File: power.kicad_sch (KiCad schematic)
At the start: 118 parts, among them IC1 STM32MP157AAB3, IC3 STC3117IJT, IC4 MCP73830T-2AAI_MYY, IC5 MT41K256M16TW-107_P, IC6 STPMIC1BPQR, IC8 STUSB1600AQTR, J1 Conn_01x04, P1 USB_C_Plug_USB2.0, Q1 PMDPB70XP_115

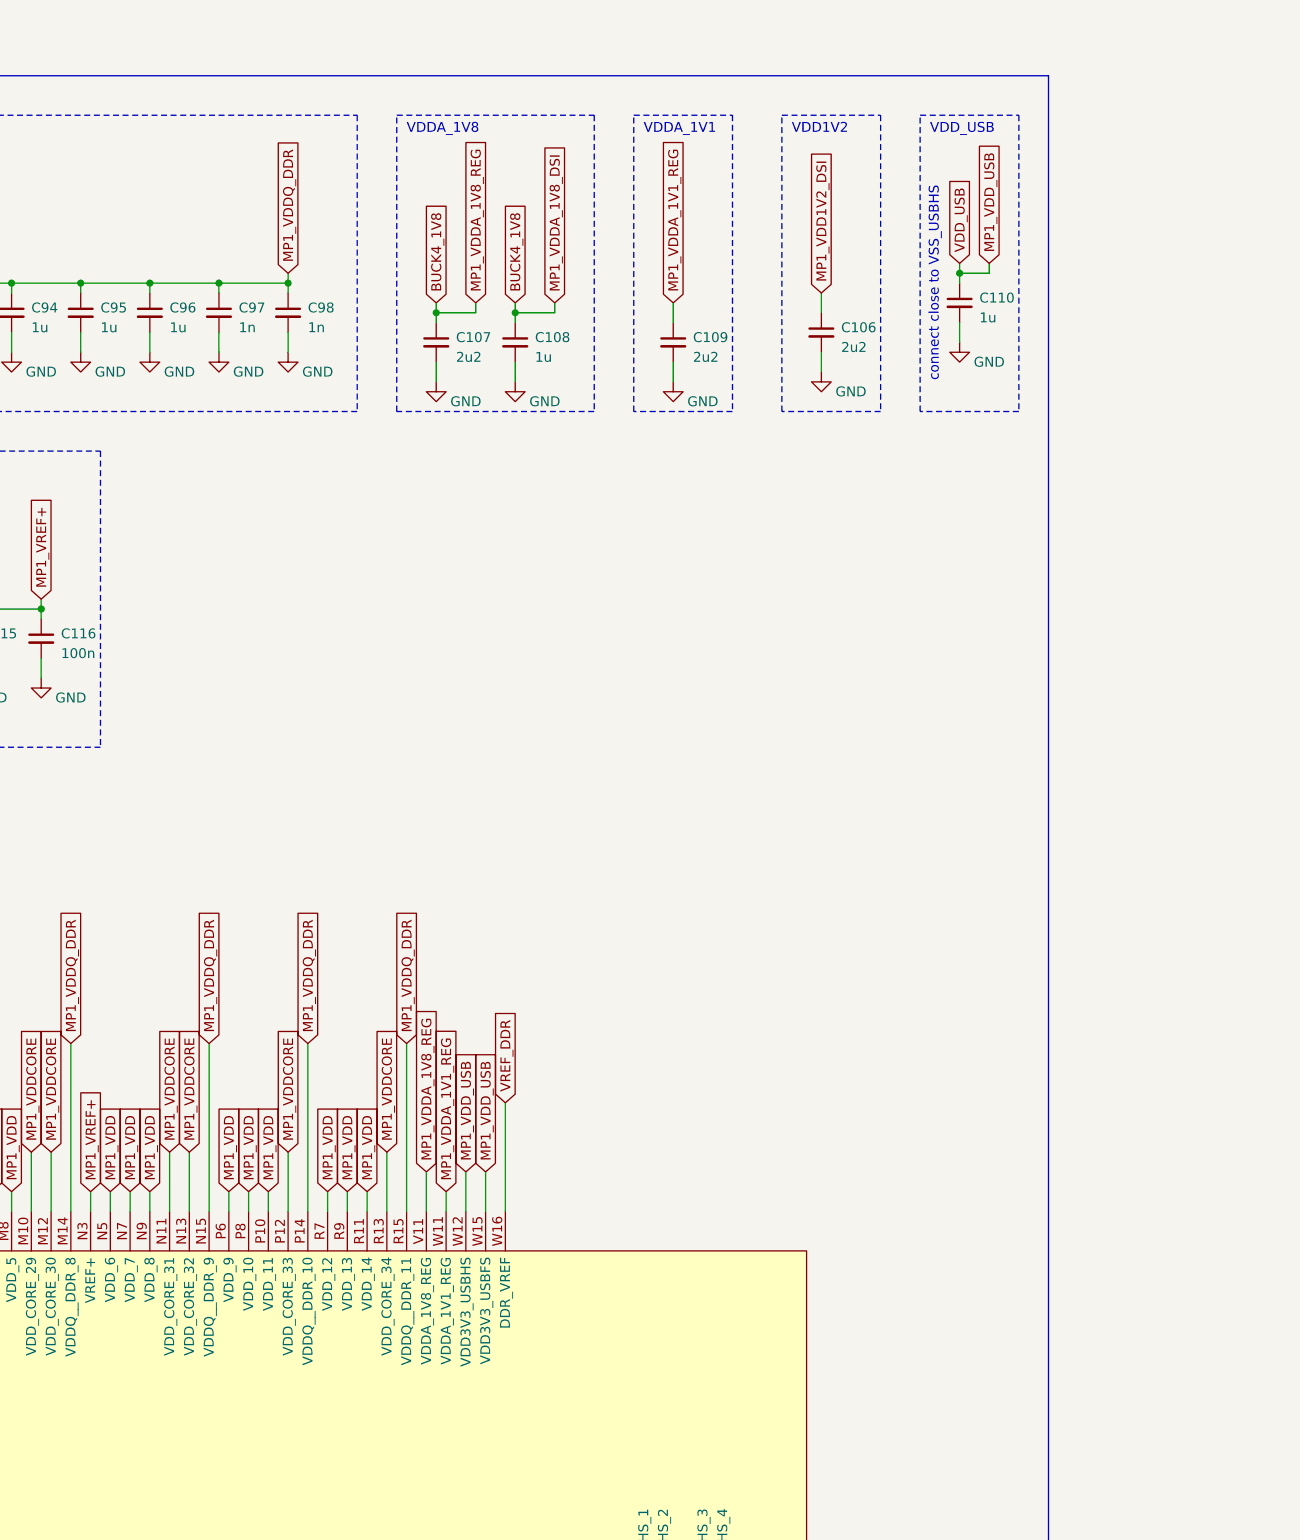
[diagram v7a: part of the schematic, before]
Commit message: changed mp1 symbol and moved BYPASS_REG1V8 signal to supply
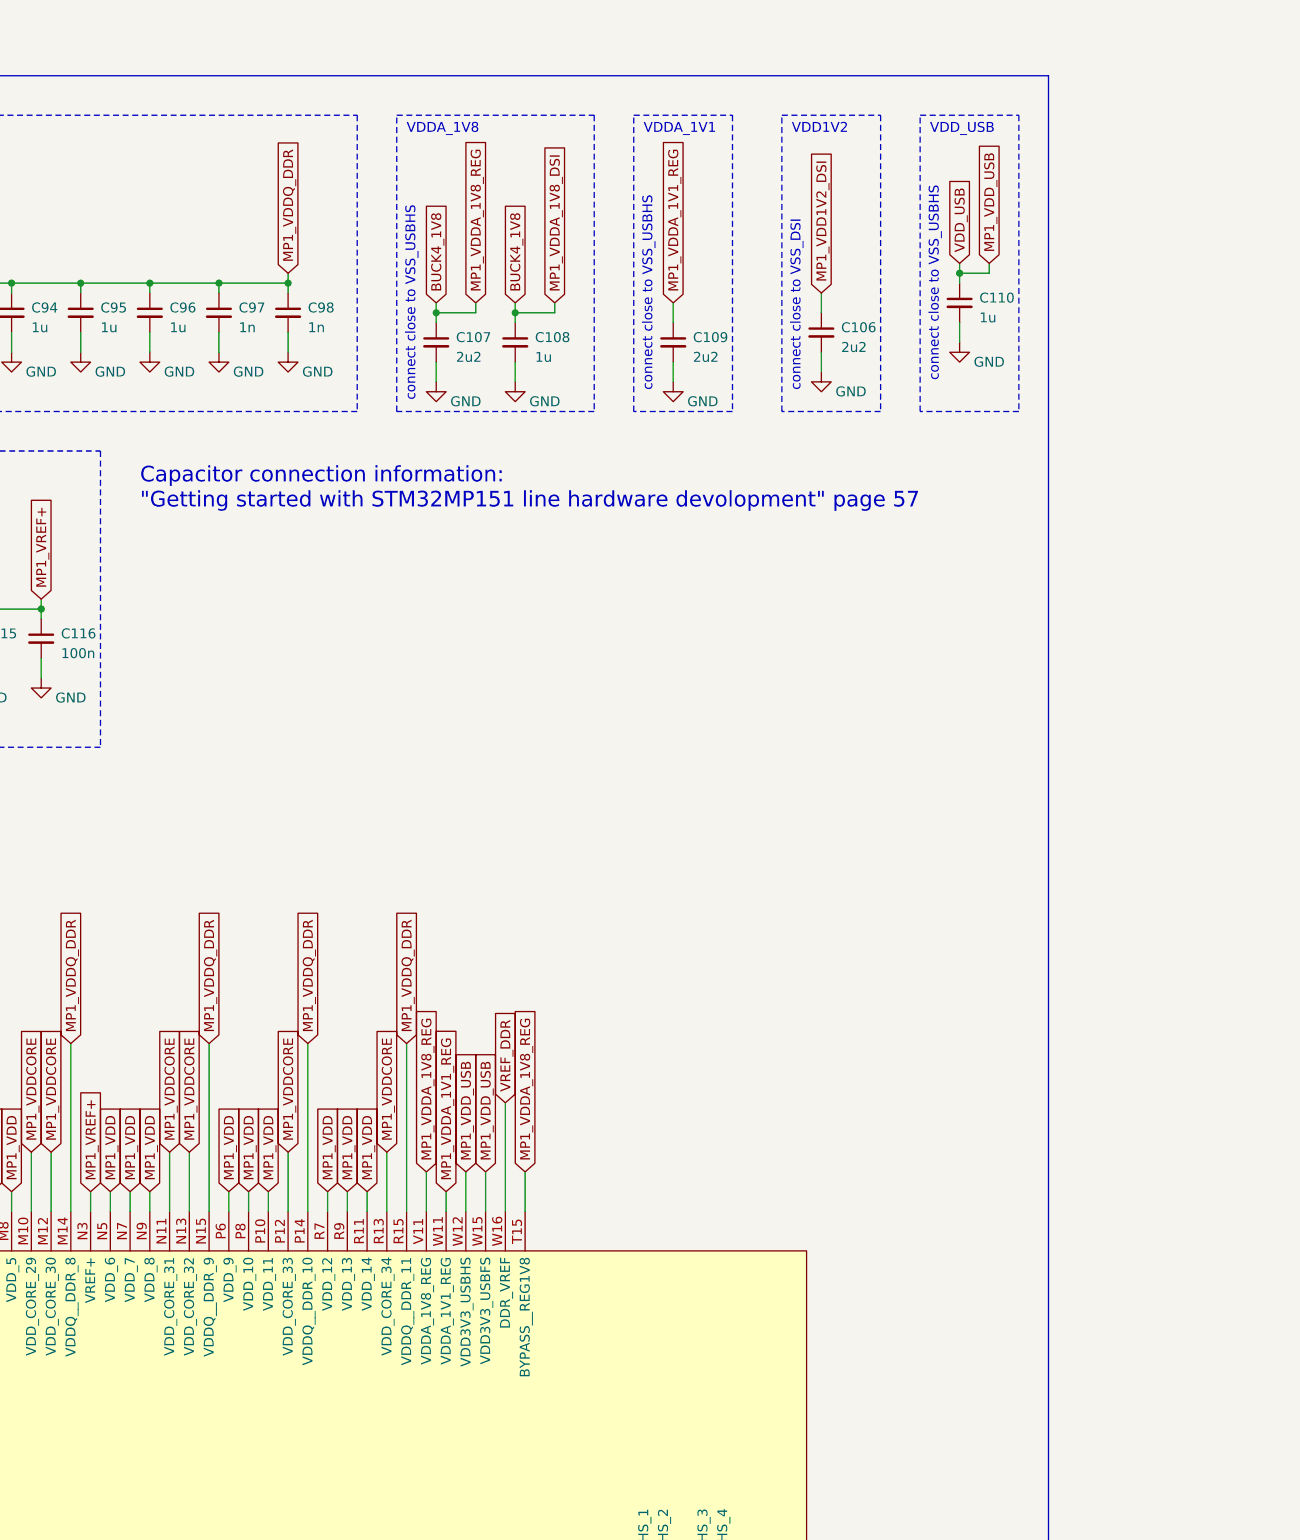
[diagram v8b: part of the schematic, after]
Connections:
- net BUCK4_1V8: now also IC1.T15 (BYPASS__REG1V8)
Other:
- note added: "Capacitor connection information: "Getting started with STM32MP151 line hardware devolopment" page 57"
- note added: "connect close to VSS_DSI"
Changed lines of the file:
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@@
     (stroke (width 0) (type default))
   )
+  (wire (pts (xy 410.21 318.77) (xy 410.21 323.85))
+    (stroke (width 0) (type default))
+  )
   (wire (pts (xy 222.25 246.38) (xy 222.25 247.65))
     (stroke (width 0) (type default))
@@
     (effects (font (size 1.27 1.27)) (justify left bottom))
   )
+  (text "connect close to VSS_USBHS" (at 396.24 219.71 90)
+    (effects (font (size 1.27 1.27)) (justify left bottom))
+  )
   (text "VDD1V2" (at 444.5 185.42 0)
     (effects (font (size 1.27 1.27)) (justify left bottom))
@@
     (effects (font (size 1.27 1.27)) (justify left bottom))
   )
+  (text "connect close to VSS_DSI" (at 445.77 218.44 90)
+    (effects (font (size 1.27 1.27)) (justify left bottom))
+  )
   (text "TODO: change to 1V8\nuse BUCK4, since it can supply 2A"
     (at 123.19 229.87 0)
@@
     (effects (font (size 1.27 1.27)) (justify left bottom))
   )
+  (text "Capacitor connection information:\n\"Getting started with STM32MP151 line hardware devolopment\" page 57"
+    (at 360.68 233.68 0)
+    (effects (font (size 2 2) (color 255 180 51 1)) (justify left bottom))
+  )
   (text "Li-Ion Battery + Gas Gauge" (at 255.27 91.44 0)
     (effects (font (size 1.27 1.27)) (justify left bottom))
@@
     (effects (font (size 1.27 1.27)) (justify left bottom))
   )
+  (text "connect close to VSS_USBHS" (at 426.72 218.44 90)
+    (effects (font (size 1.27 1.27)) (justify left bottom))
+  )
   (text "currently unused!" (at 137.16 328.93 0)
     (effects (font (size 1.27 1.27) (color 255 0 24 1)) (justify left bottom))
@@
     )
   )
+  (global_label "MP1_VDDA_1V8_REG" (shape input) (at 410.21 318.77 90) (fields_autoplaced)
+    (effects (font (size 1.27 1.27)) (justify left))
+    (property "Intersheetrefs" "${INTERSHEET_REFS}" (at 410.21 297.1167 90)
+      (effects (font (size 1.27 1.27)) (justify left) hide)
+    )
+  )
   (global_label "MP1_VDDCORE" (shape input) (at 295.91 316.23 90) (fields_autoplaced)
     (effects (font (size 1.27 1.27)) (justify left))
@@
     (pin "T13")
     (pin "T14")
-    (pin "T15")
     (pin "T16")
     (pin "T17")
@@
     (pin "R8")
     (pin "R9")
+    (pin "T15")
     (pin "T4")
     (pin "U13")
